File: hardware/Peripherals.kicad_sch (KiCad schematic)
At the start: 2 parts

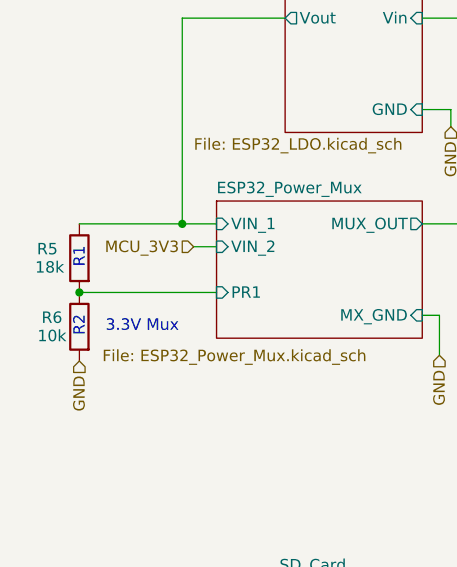
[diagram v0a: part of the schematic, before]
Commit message: added 12V buck boost
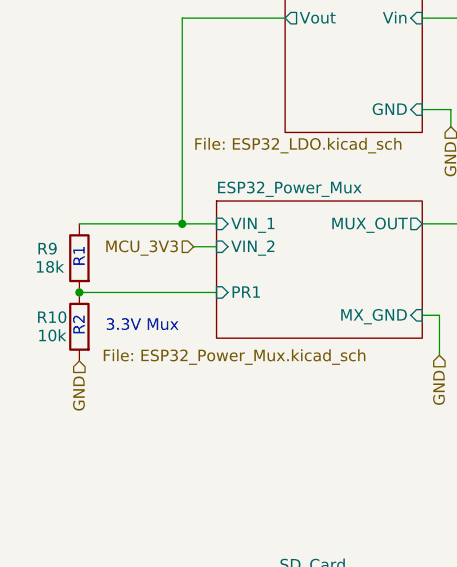
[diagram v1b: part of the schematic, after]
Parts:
- renumbered R6 to R10, R5 to R9
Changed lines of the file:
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@@
 		(in_pos_files yes)
 		(dnp no)
-		(property "Reference" "R5"
+		(property "Reference" "R9"
 			(at 18.034 113.284 0)
 			(show_name no)
@@
 			(project "PS-BPSLeader"
 				(path "/d4a4ed4f-0983-4aef-b212-0e3284ab3963/5da56964-fa04-4fec-bdfe-c6acfeda5c9a"
-					(reference "R5")
+					(reference "R9")
 					(unit 1)
 				)
@@
 		(in_pos_files yes)
 		(dnp no)
-		(property "Reference" "R6"
+		(property "Reference" "R10"
 			(at 18.542 120.904 0)
 			(show_name no)
@@
 			(project "PS-BPSLeader"
 				(path "/d4a4ed4f-0983-4aef-b212-0e3284ab3963/5da56964-fa04-4fec-bdfe-c6acfeda5c9a"
-					(reference "R6")
+					(reference "R10")
 					(unit 1)
 				)

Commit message: forgot to push last night
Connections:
- no-connect marks 43 -> 41

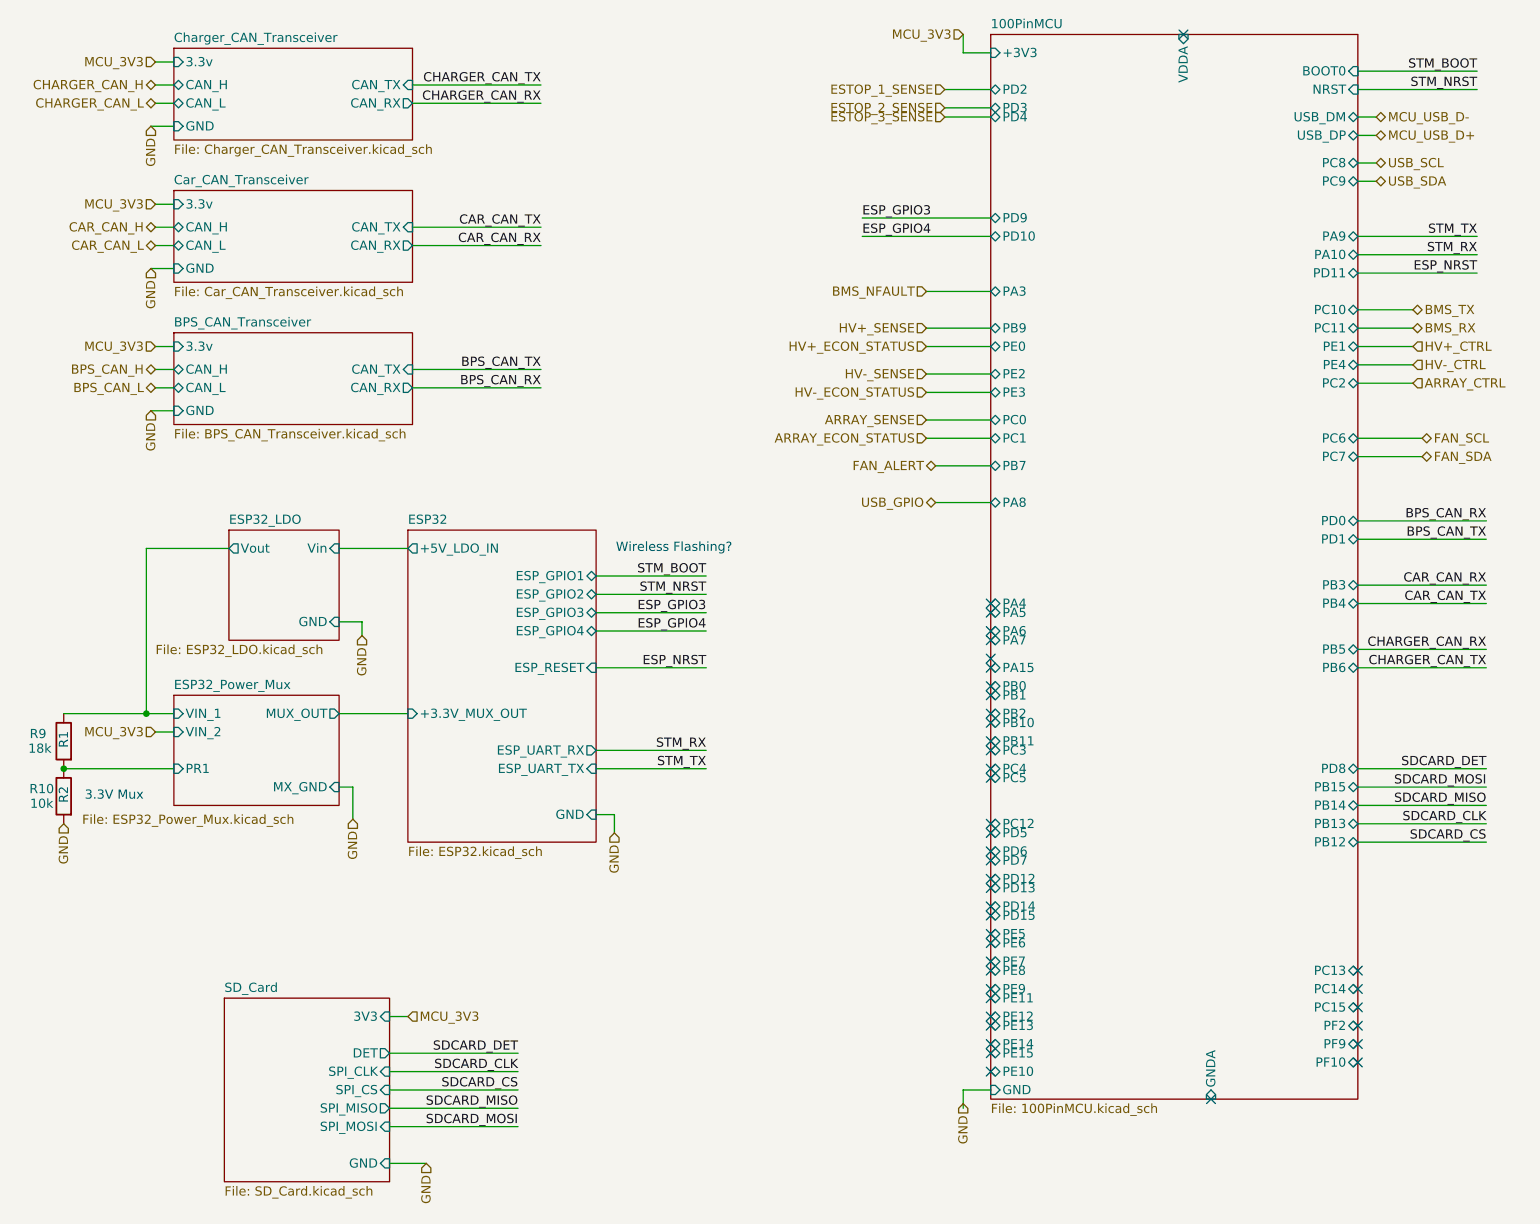
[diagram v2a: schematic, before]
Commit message: kms drc crashed and didn't save layout
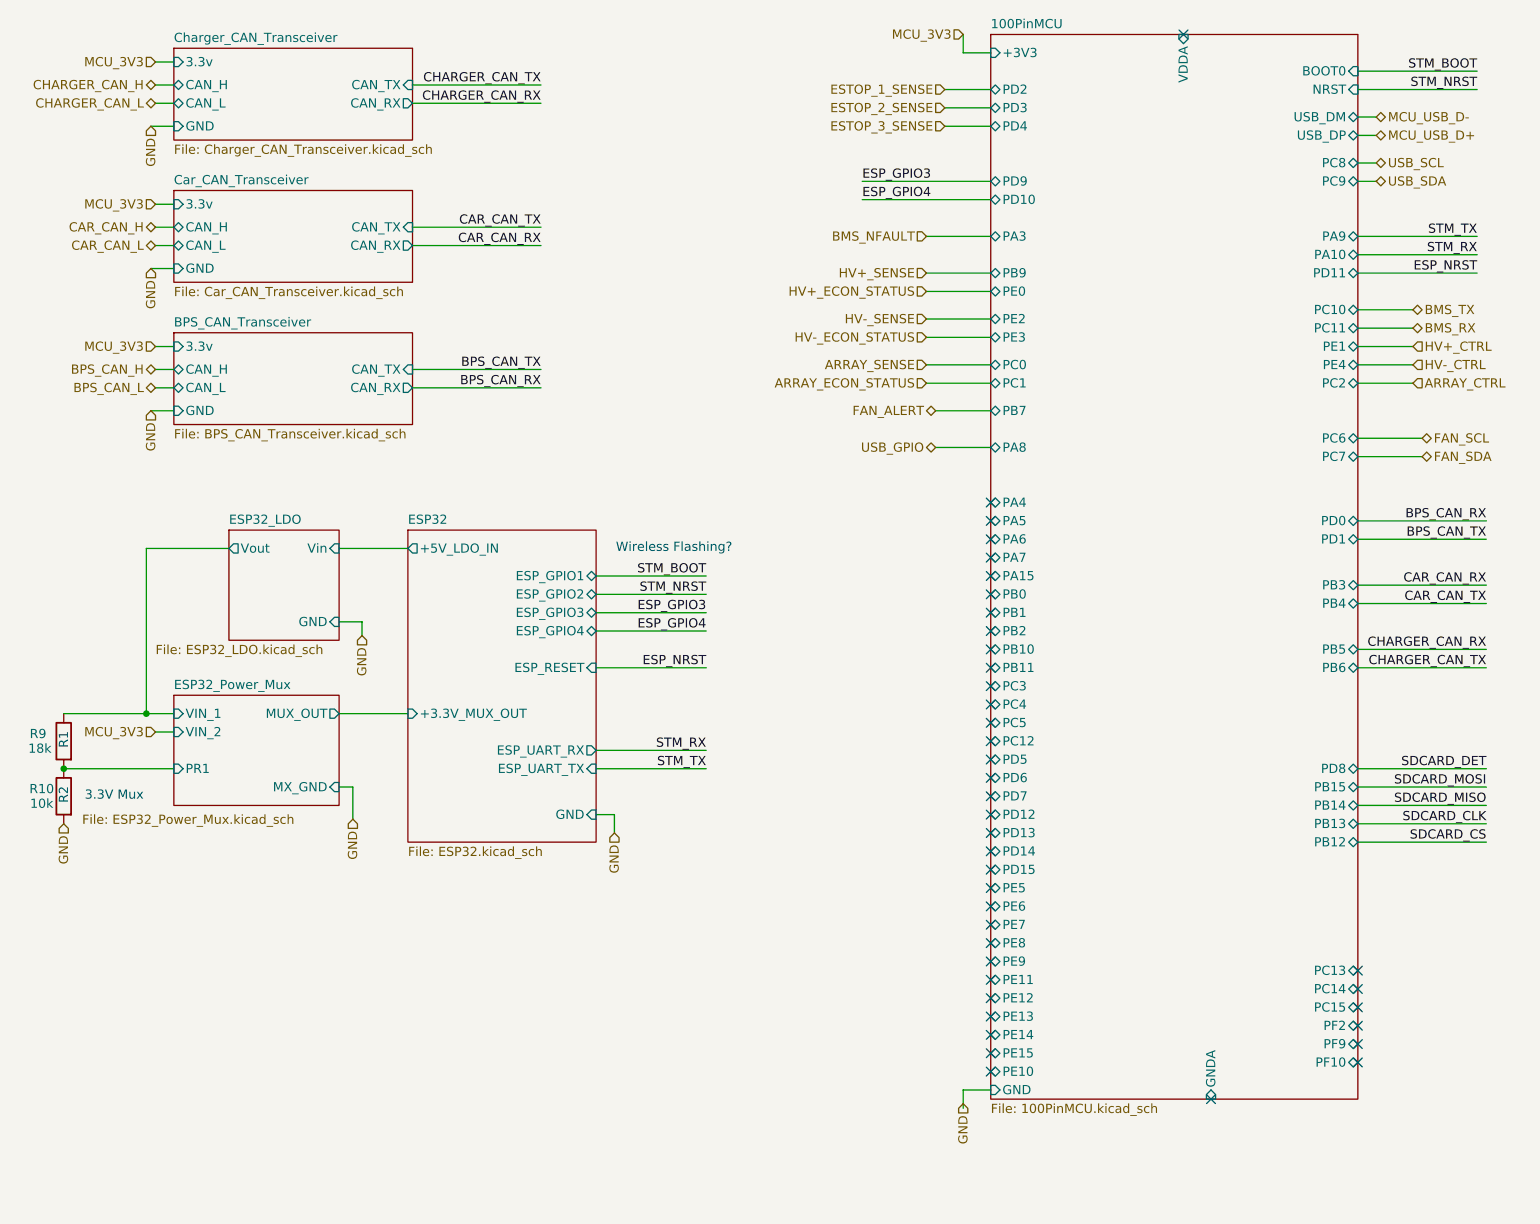
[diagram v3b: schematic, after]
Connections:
- no-connect marks 41 -> 40
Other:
- removed sheet SD_Card

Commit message: papercut -linkin park
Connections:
- no-connect marks 40 -> 45
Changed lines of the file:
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@@
+	)
+	(no_connect
+		(at 200.66 118.11)
 	)
 	(no_connect
@@
 	)
 	(no_connect
+		(at 200.66 120.65)
+	)
+	(no_connect
+		(at 200.66 128.27)
+	)
+	(no_connect
 		(at 149.86 96.52)
 	)
 	(no_connect
+		(at 200.66 123.19)
+	)
+	(no_connect
 		(at 149.86 142.24)
 	)
@@
 	)
 	(no_connect
+		(at 200.66 125.73)
+	)
+	(no_connect
 		(at 149.86 106.68)
 	)
@@
 	(wire
 		(pts
+			(xy 146.05 162.56) (xy 146.05 165.1)
+		)
+		(stroke
+			(width 0)
+			(type default)
+		)
+	)
+	(wire
+		(pts
 			(xy 200.66 57.15) (xy 208.28 57.15)
 		)
@@
 	(wire
 		(pts
-			(xy 200.66 123.19) (xy 218.44 123.19)
-		)
-		(stroke
-			(width 0)
-			(type default)
-		)
-	)
-	(wire
-		(pts
 			(xy 62.865 99.695) (xy 62.865 97.79)
 		)
@@
 	(wire
 		(pts
-			(xy 200.66 118.11) (xy 218.44 118.11)
-		)
-		(stroke
-			(width 0)
-			(type default)
-		)
-	)
-	(wire
-		(pts
 			(xy 200.66 36.83) (xy 203.2 36.83)
 		)
@@
 	(wire
 		(pts
-			(xy 218.44 128.27) (xy 200.66 128.27)
-		)
-		(stroke
-			(width 0)
-			(type default)
-		)
-	)
-	(wire
-		(pts
 			(xy 140.97 52.07) (xy 149.86 52.07)
 		)
@@
 	(wire
 		(pts
-			(xy 200.66 120.65) (xy 218.44 120.65)
-		)
-		(stroke
-			(width 0)
-			(type default)
-		)
-	)
-	(wire
-		(pts
 			(xy 87.63 45.72) (xy 69.85 45.72)
 		)
@@
 	(wire
 		(pts
-			(xy 146.05 165.1) (xy 146.05 162.56)
-		)
-		(stroke
-			(width 0)
-			(type default)
-		)
-	)
-	(wire
-		(pts
 			(xy 200.66 72.39) (xy 209.55 72.39)
 		)
@@
 		(pts
 			(xy 200.66 104.14) (xy 218.44 104.14)
-		)
-		(stroke
-			(width 0)
-			(type default)
-		)
-	)
-	(wire
-		(pts
-			(xy 200.66 125.73) (xy 218.44 125.73)
 		)
 		(stroke
@@
 		)
 	)
-	(label "SDCARD_MISO"
-		(at 218.44 123.19 180)
-		(effects
-			(font
-				(size 1.27 1.27)
-			)
-			(justify right bottom)
-		)
-	)
 	(label "CAR_CAN_RX"
 		(at 218.44 92.71 180)
@@
 		)
 	)
-	(label "SDCARD_DET"
-		(at 218.44 118.11 180)
-		(effects
-			(font
-				(size 1.27 1.27)
-			)
-			(justify right bottom)
-		)
-	)
 	(label "CHARGER_CAN_RX"
 		(at 87.63 26.035 180)
@@
 		)
 	)
-	(label "SDCARD_CS"
-		(at 218.44 128.27 180)
-		(effects
-			(font
-				(size 1.27 1.27)
-			)
-			(justify right bottom)
-		)
-	)
 	(label "BPS_CAN_RX"
 		(at 218.44 83.82 180)
@@
 		)
 	)
-	(label "SDCARD_CLK"
-		(at 218.44 125.73 180)
-		(effects
-			(font
-				(size 1.27 1.27)
-			)
-			(justify right bottom)
-		)
-	)
 	(label "STM_RX"
 		(at 110.49 115.57 180)
-		(effects
-			(font
-				(size 1.27 1.27)
-			)
-			(justify right bottom)
-		)
-	)
-	(label "SDCARD_MOSI"
-		(at 218.44 120.65 180)
 		(effects
 			(font
@@
 		)
 	)
-	(hierarchical_label "ARRAY_ECON_STATUS"
+	(hierarchical_label "MOTOR_ECON_STATUS"
 		(shape input)
 		(at 140.97 64.77 180)
@@
 	(hierarchical_label "GND"
 		(shape input)
-		(at 146.05 164.465 270)
+		(at 146.05 165.1 270)
 		(effects
 			(font
@@
 		)
 	)
-	(hierarchical_label "ARRAY_CTRL"
+	(hierarchical_label "MOTOR_CTRL"
 		(shape input)
 		(at 208.28 64.77 0)
@@
 		)
 	)
-	(hierarchical_label "ARRAY_SENSE"
+	(hierarchical_label "MOTOR_SENSE"
 		(shape input)
 		(at 140.97 62.23 180)
